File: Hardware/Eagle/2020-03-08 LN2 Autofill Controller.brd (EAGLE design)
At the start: 114.3 x 95.2 mm, 28 parts, among them SW1 Omron B3J-2100, SW2 Omron B3J-2100, SW3 Omron B3J-2100, SW4 Omron B3J-2100, U1 MC14490DWG, U3 ISO7421DR

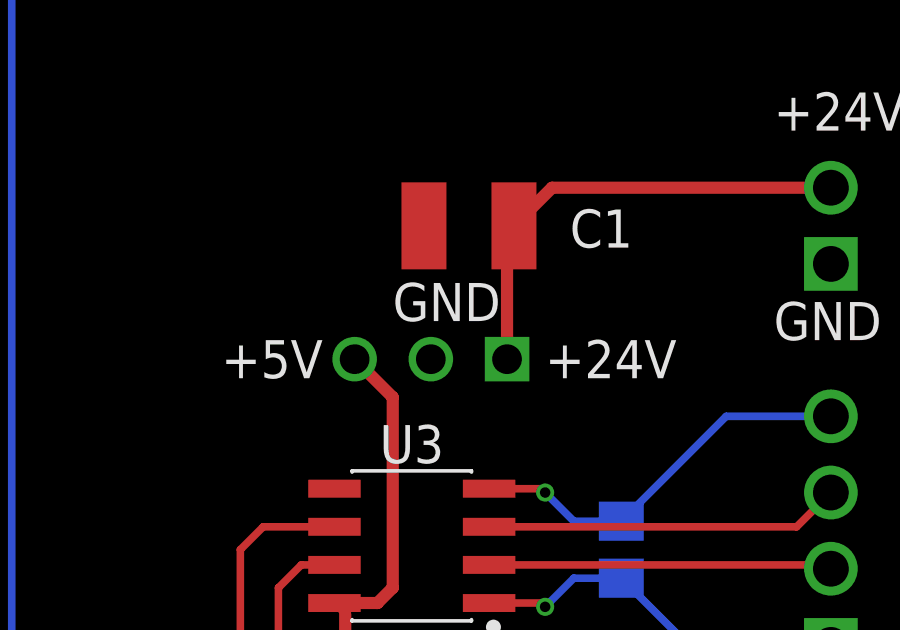
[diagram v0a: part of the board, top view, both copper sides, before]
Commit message: Swapped 5VDC convert to stand-up version
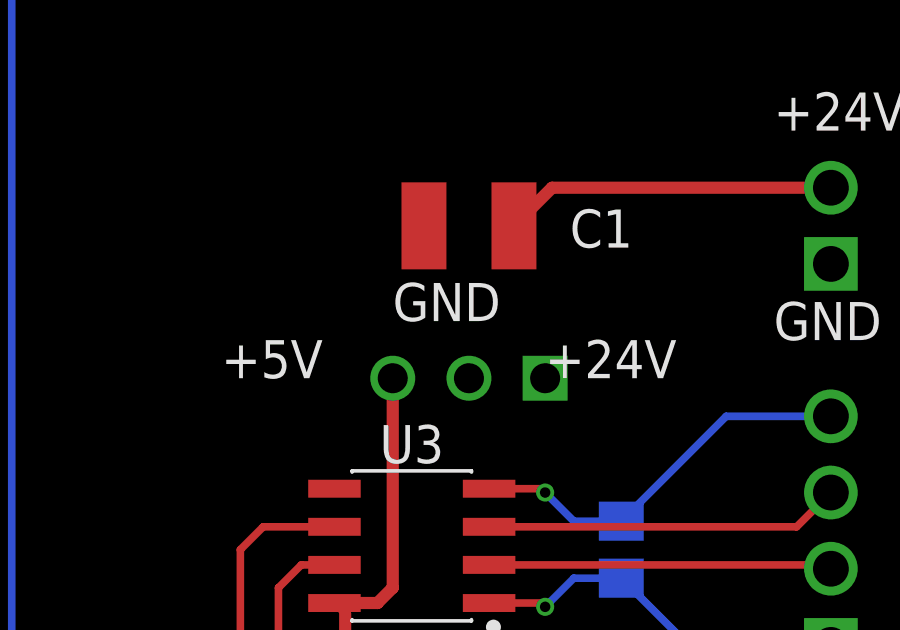
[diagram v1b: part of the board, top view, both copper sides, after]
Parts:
- removed VR1: OKI-78SR-5, AUmlib:OKI-78SR
- added PS2: OKI-78SR-5/1.5-W36-C, AUmlib:CONV_OKI-78SR-5/1.5-W36-C
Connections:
- new net VOUT: PS2.3
- net +24V: now also PS2.1; no longer VR1.VIN
- net +5V: no longer VR1.VOUT
- net GND: now also PS2.2; no longer VR1.GND
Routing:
- net +24V: track 15.6 -> 11.4 mm
- net +5V: track 31.1 -> 29.3 mm
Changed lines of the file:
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@@
 </element>
 <element name="CNANO1" library="AUmlib" library_urn="urn:adsk.eagle:library:9166017" package="CURIOSITYNANO4809CASTELLATED" package3d_urn="urn:adsk.eagle:package:15461731/6" value="CURIOSITYNANO4809CASTELLATED" x="72.39" y="19.05" smashed="yes" rot="R270"/>
-<element name="VR1" library="AUmlib" library_urn="urn:adsk.eagle:library:9166017" package="OKI-78SR" package3d_urn="urn:adsk.eagle:package:23154151/4" value="OKI-78SR-5" x="95.25" y="46.355" smashed="yes" rot="MR0">
-<attribute name="NAME" x="89.535" y="41.91" size="1.27" layer="26" font="vector" rot="MR180"/>
-</element>
 <element name="C1" library="AUmlib" library_urn="urn:adsk.eagle:library:9166017" package="C1210K" package3d_urn="urn:adsk.eagle:package:4021329/2" value="10uF" x="96.52" y="50.8" smashed="yes" rot="R180">
 <attribute name="NAME" x="99.885" y="50.075" size="1.27" layer="25" font="vector"/>
@@
 <element name="TP1" library="AUmlib" library_urn="urn:adsk.eagle:library:9166017" package="TESTPOINT1" package3d_urn="urn:adsk.eagle:package:15845500/3" value="" x="13.97" y="8.255" smashed="yes" rot="MR180"/>
 <element name="TP2" library="AUmlib" library_urn="urn:adsk.eagle:library:9166017" package="TESTPOINT1" package3d_urn="urn:adsk.eagle:package:15845500/3" value="" x="6.985" y="8.255" smashed="yes" rot="MR0"/>
+<element name="PS2" library="AUmlib" library_urn="urn:adsk.eagle:library:9166017" package="CONV_OKI-78SR-5/1.5-W36-C" package3d_urn="urn:adsk.eagle:package:24308288/2" value="OKI-78SR-5/1.5-W36-C" x="96.52" y="45.72" smashed="yes" rot="MR0">
+<attribute name="DESCRIPTION" value=" Linear Regulator Replacement DC DC Converter 1 Output 5V 1.5A 7V - 36V Input " x="96.52" y="45.72" size="1.778" layer="28" rot="MR0" display="off"/>
+<attribute name="DIGI-KEY_PART_NUMBER" value="811-2196-5-ND" x="96.52" y="45.72" size="1.778" layer="28" rot="MR0" display="off"/>
+<attribute name="MF" value="Murata Power Solutions Inc." x="96.52" y="45.72" size="1.778" layer="28" rot="MR0" display="off"/>
+<attribute name="MP" value="OKI-78SR-5/1.5-W36-C" x="96.52" y="45.72" size="1.778" layer="28" rot="MR0" display="off"/>
+<attribute name="NAME" x="101.52" y="51.72" size="1" layer="26" rot="MR0"/>
+<attribute name="PACKAGE" value="SIP-3 Murata Power" x="96.52" y="45.72" size="1.778" layer="28" rot="MR0" display="off"/>
+<attribute name="PURCHASE-URL" value="https://pricing.snapeda.com/search/part/OKI-78SR-5/1.5-W36-C/?ref=eda" x="96.52" y="45.72" size="1.778" layer="28" rot="MR0" display="off"/>
+<attribute name="VALUE" x="101.52" y="40.72" size="1" layer="28" rot="MR0"/>
+</element>
 </elements>
 <signals>
@@
 <contactref element="JP2" pad="7"/>
 <contactref element="JP2" pad="14"/>
-<contactref element="VR1" pad="GND"/>
 <contactref element="C2" pad="2"/>
 <contactref element="SW3" pad="3"/>
@@
 <contactref element="CNANO1" pad="VOFF"/>
 <contactref element="PS1" pad="6"/>
+<contactref element="PS2" pad="2"/>
 </signal>
 <signal name="+5V">
 <contactref element="JP2" pad="13"/>
-<contactref element="VR1" pad="VOUT"/>
 <contactref element="PS1" pad="1"/>
 <contactref element="C2" pad="1"/>
@@
 <wire x1="92.0375" y1="38.227" x2="93.472" y2="38.227" width="0.4064" layer="1"/>
 <wire x1="93.472" y1="38.227" x2="93.98" y2="38.735" width="0.4064" layer="1"/>
-<wire x1="93.98" y1="45.085" x2="92.71" y2="46.355" width="0.4064" layer="1"/>
 <wire x1="93.98" y1="38.735" x2="93.98" y2="45.085" width="0.4064" layer="1"/>
 <polygon width="0.254" layer="16">
@@
 <via x="47.625" y="62.865" extent="1-16" drill="0.35"/>
 <contactref element="LCD1" pad="3"/>
+<wire x1="93.98" y1="11.43" x2="92.395" y2="35.56" width="0" layer="19" extent="1-1"/>
 </signal>
 <signal name="THER4-SIG">
@@
 <signal name="+24V">
 <contactref element="C1" pad="1"/>
-<contactref element="VR1" pad="VIN"/>
 <contactref element="JP3" pad="2"/>
-<wire x1="97.79" y1="46.355" x2="97.79" y2="50.57" width="0.4064" layer="1"/>
 <wire x1="97.79" y1="50.57" x2="98.02" y2="50.8" width="0.4064" layer="1"/>
 <wire x1="98.02" y1="50.8" x2="99.29" y2="52.07" width="0.4064" layer="1"/>
 <wire x1="99.29" y1="52.07" x2="108.585" y2="52.07" width="0.4064" layer="1"/>
+<contactref element="PS2" pad="1"/>
+<wire x1="99.06" y1="45.72" x2="97.79" y2="50.57" width="0" layer="19" extent="1-1"/>
 </signal>
 <signal name="N$1">
@@
 <wire x1="35.56" y1="54.29" x2="35.56" y2="58.42" width="0.254" layer="16"/>
 </signal>
+<signal name="VOUT">
+<contactref element="PS2" pad="3"/>
+</signal>
 </signals>
